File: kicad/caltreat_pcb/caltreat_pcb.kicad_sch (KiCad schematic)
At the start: 43 parts, among them J1 Conn_01x12_Pin, J10 Conn_01x02_Pin, J11 Conn_01x02_Pin, J12 Conn_01x02_Pin, J13 Conn_01x02_Pin, J14 Conn_01x02_Pin, J15 Conn_01x02_Pin, J2 Conn_01x12_Pin, J3 Conn_01x02_Pin, J4 Conn_01x02_Pin, J5 Conn_01x02_Pin, J6 Conn_01x02_Pin, J7 Conn_01x02_Pin, J8 Conn_01x02_Pin, J9 Conn_01x02_Pin, Q1 AO3400A, Q2 AO3400A, Q3 AO3400A, Q4 AO3400A, Q5 AO3400A, Q6 AO3400A, Q7 AO3400A, Q8 AO3400A

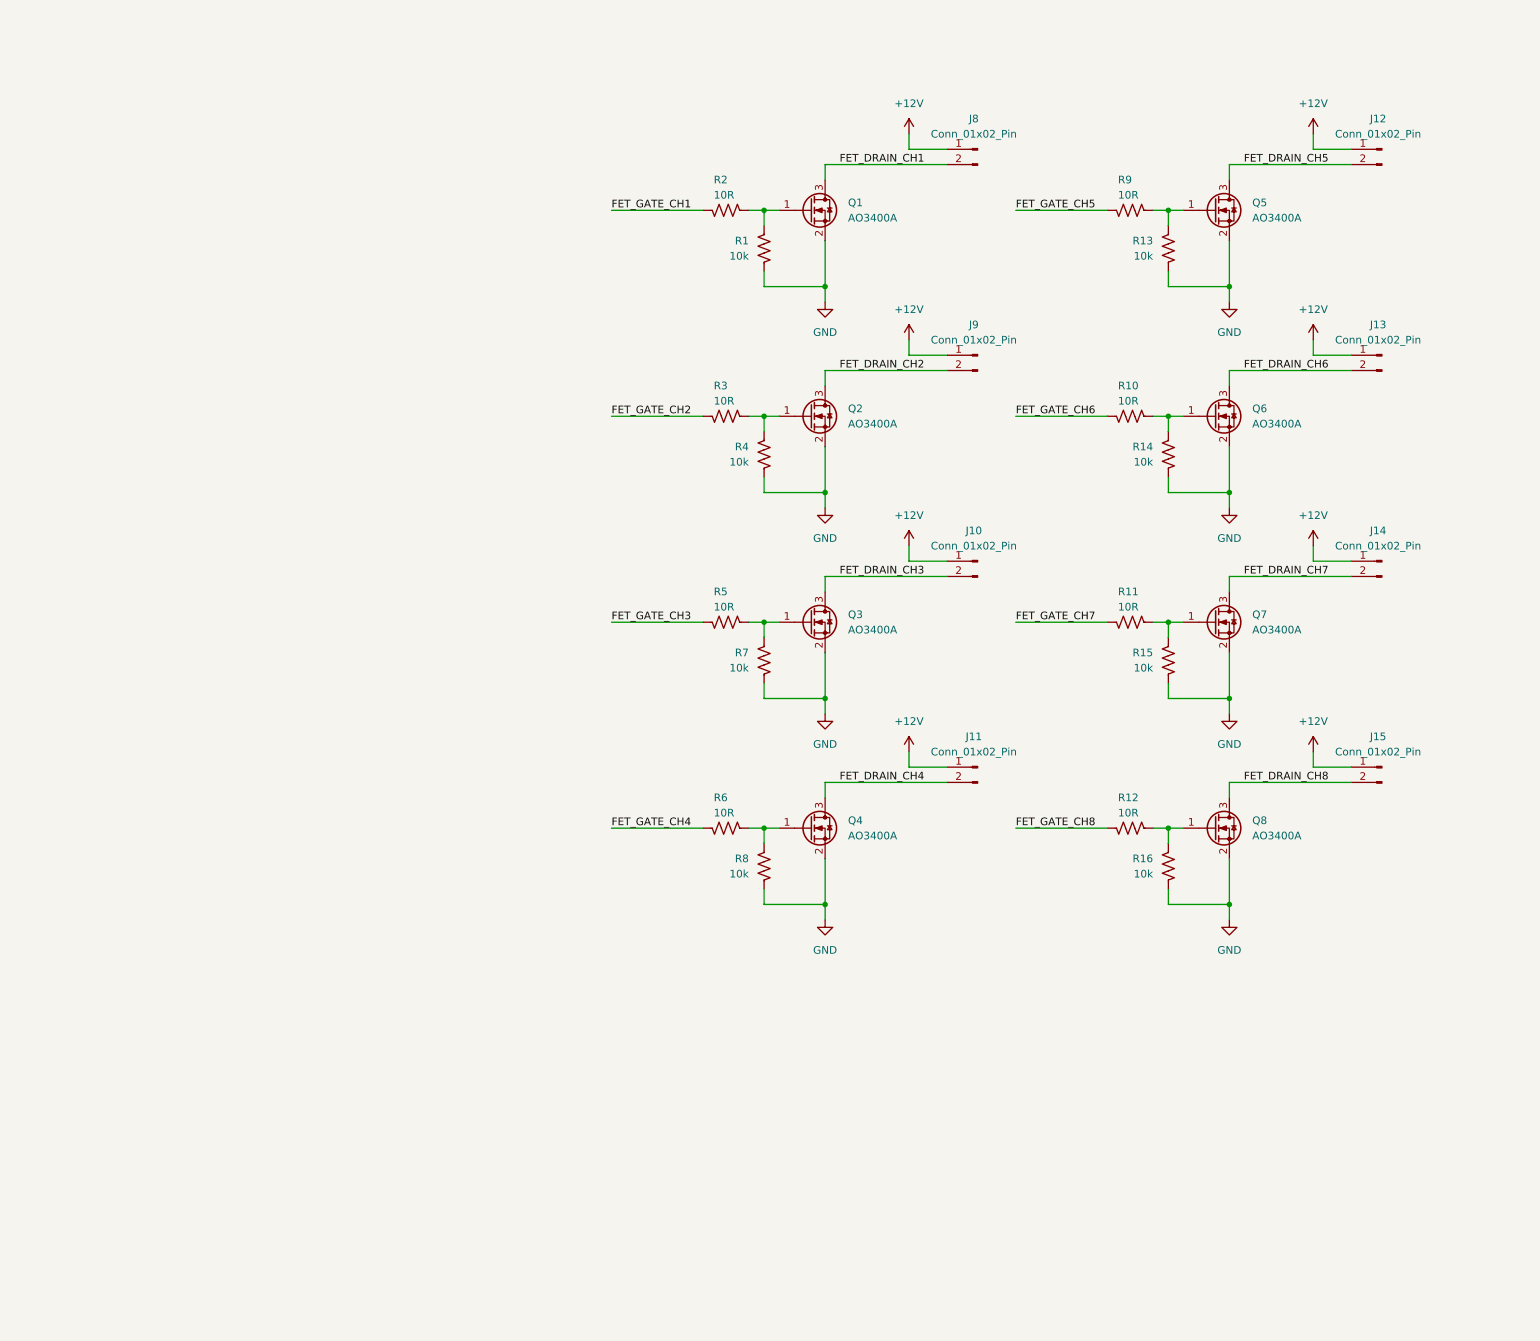
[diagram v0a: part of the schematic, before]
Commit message: Add level crossing signal firmware
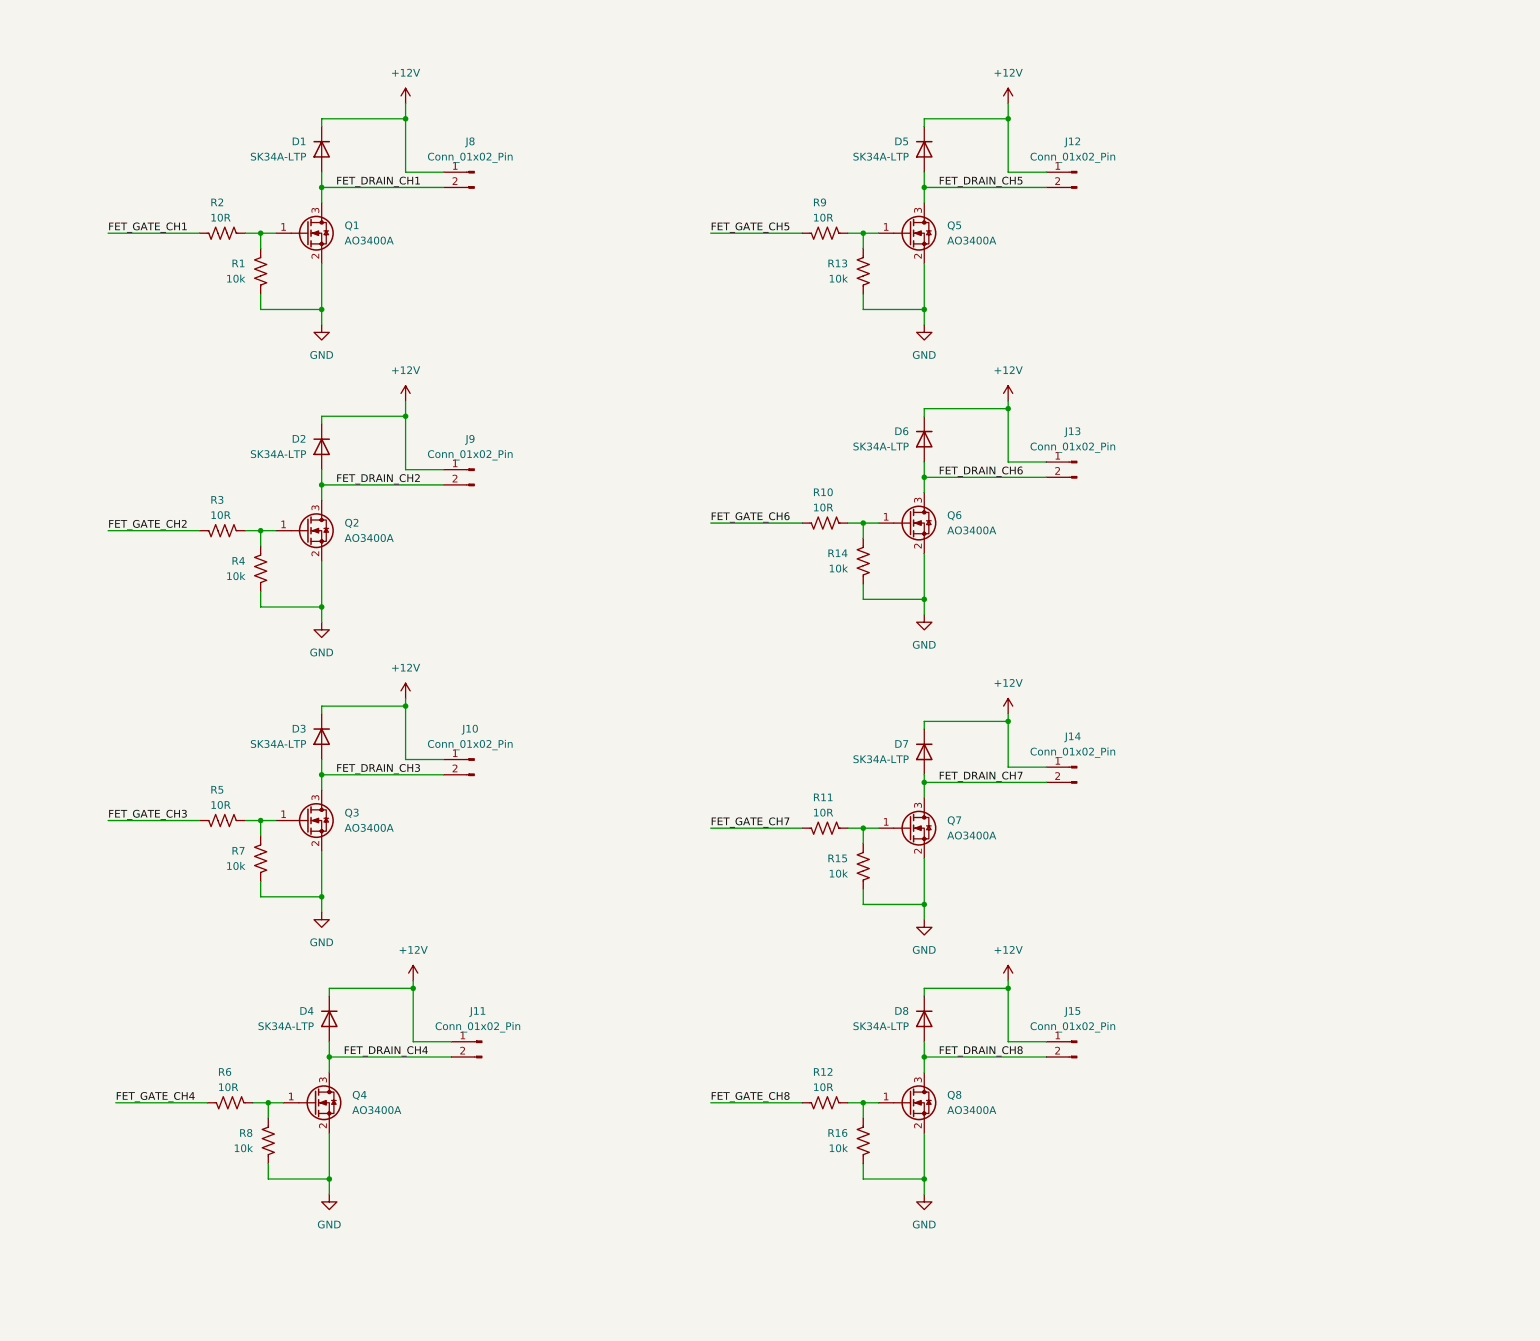
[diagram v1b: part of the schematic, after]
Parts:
- added D1, D2, D3, D4, D5, D6, D7, D8: SK34A-LTP, Diode_SMD:D_SMA, symbol Device:D
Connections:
- net +12V: now also D1.1 (K), D2.1 (K), D3.1 (K), D4.1 (K), D5.1 (K), D6.1 (K), D7.1 (K), D8.1 (K)
- net FET_DRAIN_CH1: now also D1.2 (A)
- net FET_DRAIN_CH2: now also D2.2 (A)
- net FET_DRAIN_CH3: now also D3.2 (A)
- net FET_DRAIN_CH4: now also D4.2 (A)
- net FET_DRAIN_CH5: now also D5.2 (A)
- net FET_DRAIN_CH6: now also D6.2 (A)
- net FET_DRAIN_CH7: now also D7.2 (A)
- net FET_DRAIN_CH8: now also D8.2 (A)
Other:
- moved on the sheet: J10, J11, J12, J13, J14, J15, J8, J9, Q1, Q2, Q3, Q4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
